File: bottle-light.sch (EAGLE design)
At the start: 49 parts, among them IC1 STM32F334K8T, IC2 LF33, T1 BC337, T2 BC337, T3 BC337

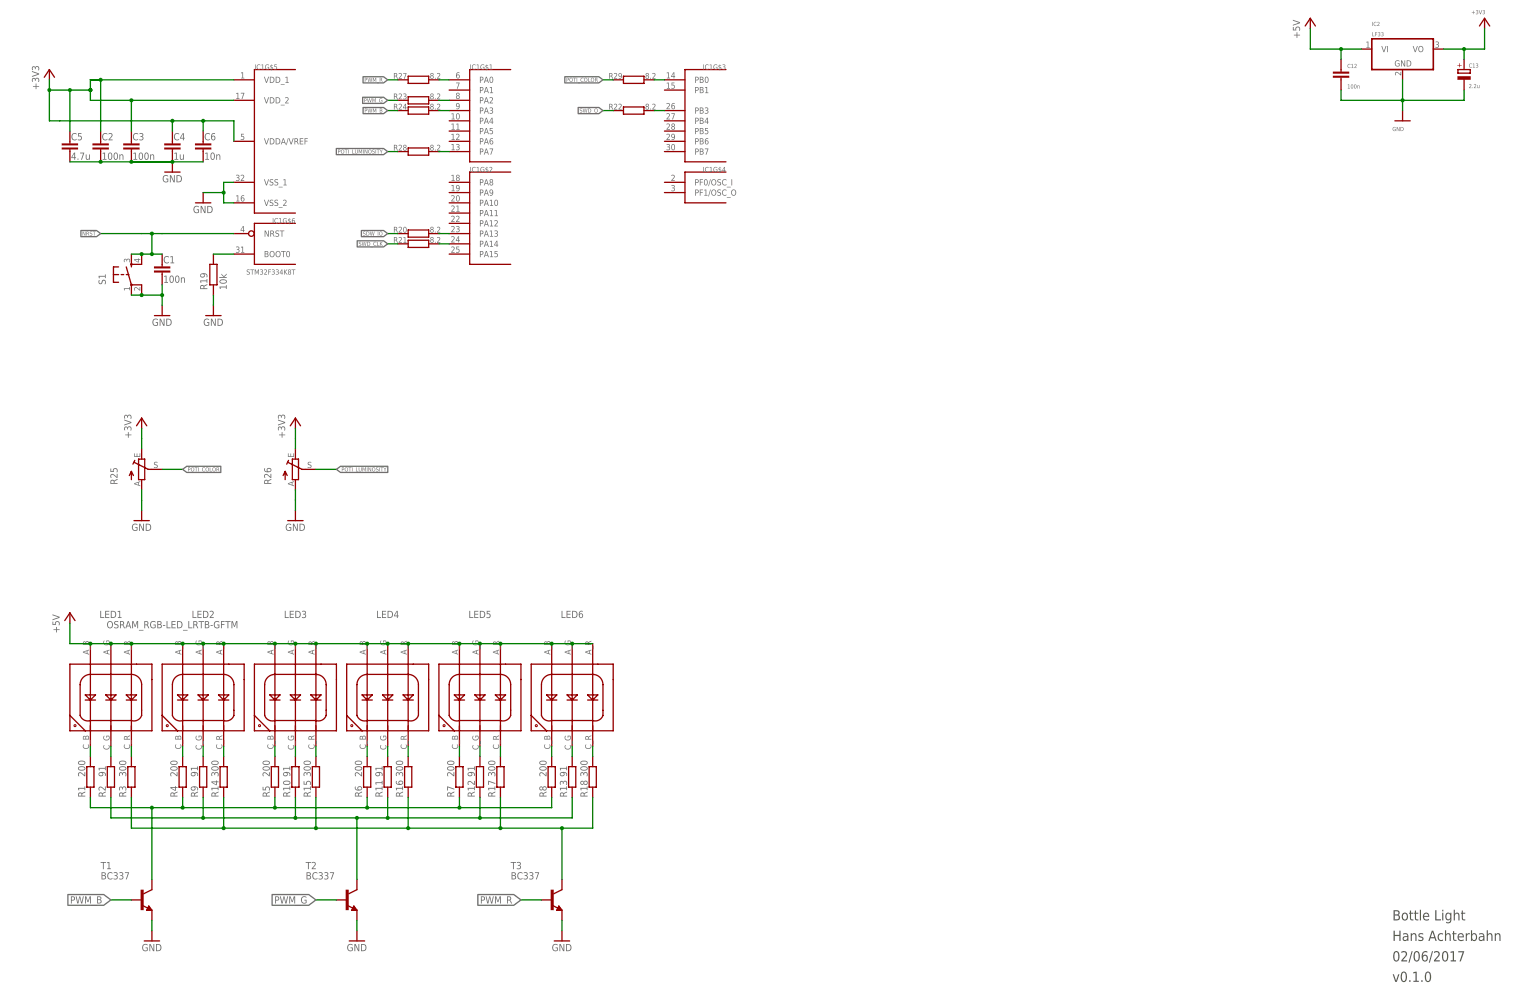
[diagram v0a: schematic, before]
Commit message: v0.1.1 worked on circuit diagram - new push buttons - new on/off button
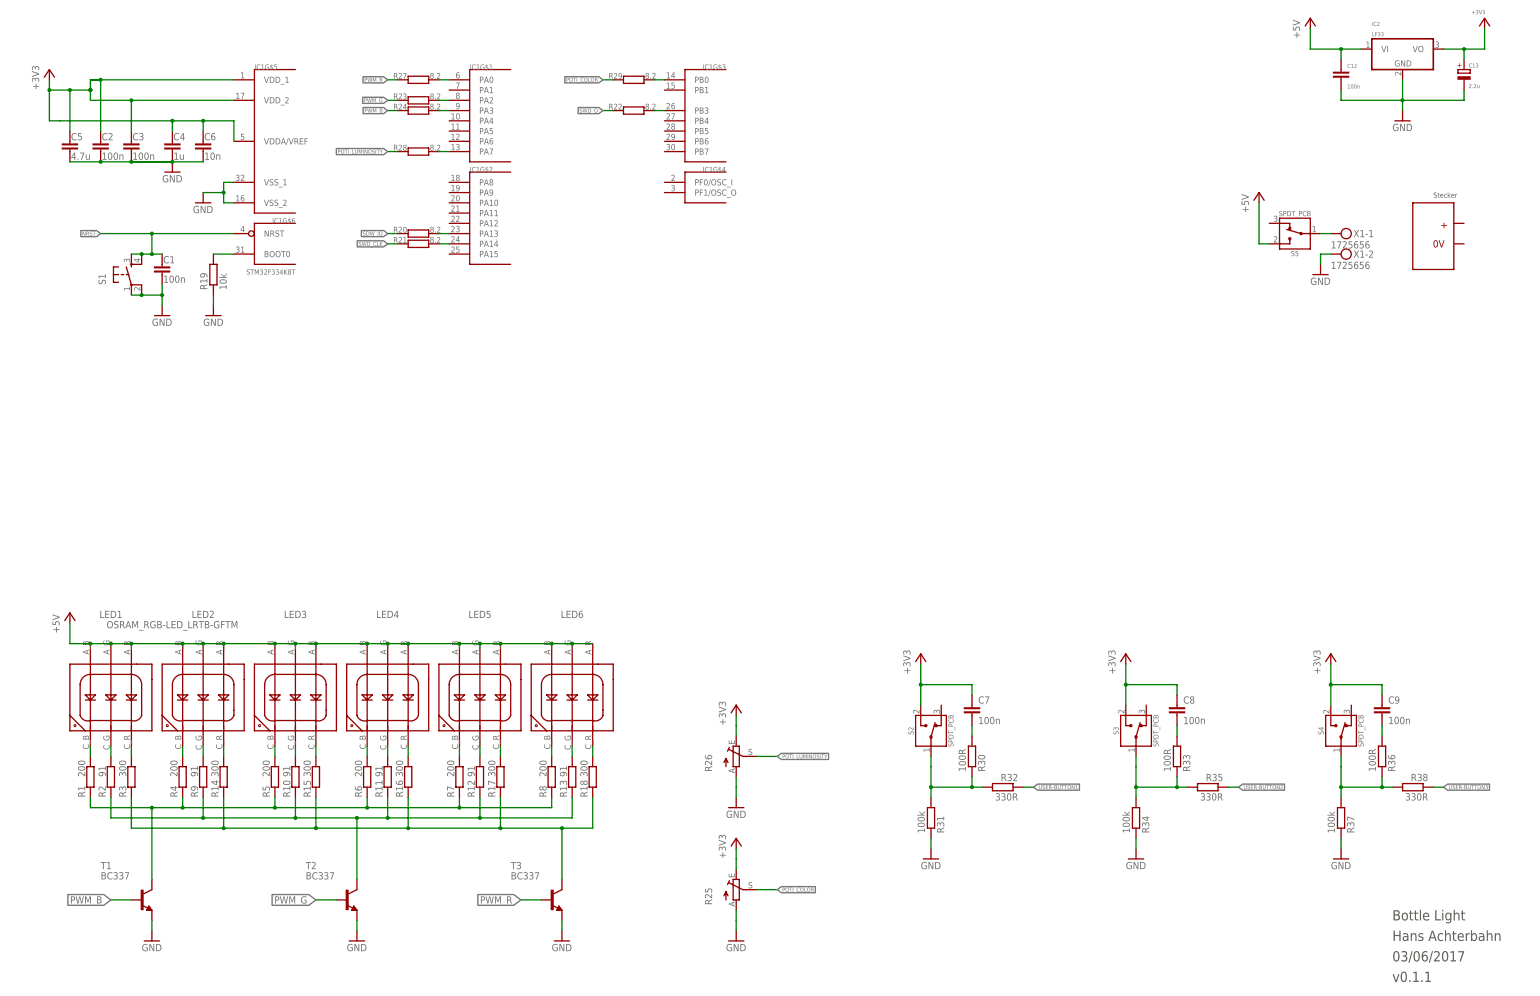
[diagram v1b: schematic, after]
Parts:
- added C7, C8, C9: 100n, resistor:C-EUC0603
- added R30, R33, R36: 100R, rcl:R-EU_R0603
- added R31, R34, R37: 100k, rcl:R-EU_R0603
- added R32, R35, R38: 330R, rcl:R-EU_R0603
- added S2, S3, S4, S5: SPDT_PCB, h8-switch:SPDT_PCB
- added X1: 1725656, con-phoenix-508:MKDSN1,5/2-5,08
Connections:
- new net N$30: R30.1, R31.2, R32.2, S2.1
- new net N$31: C7.2, R30.2
- new net N$32: R33.1, R34.2, R35.2, S3.1
- new net N$33: C8.2, R33.2
- new net N$35: R36.1, R37.2, R38.2, S4.1
- new net N$36: C9.2, R36.2
- new net N$37: S5.1, X1-1.KL
- new net USER-BUTTON1: R32.1
- new net USER-BUTTON2: R35.1
- new net USER-BUTTON3: R38.1
- net +3V3: now also C7.1, C8.1, C9.1, S2.2, S3.2, S4.2
- net +5V: now also S5.2
- net GND: now also R31.1, R34.1, R37.1, X1-2.KL
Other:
- note added: "03/06/2017"
- note added: "Stecker"
- note added: "v0.1.1"
- note removed: "02/06/2017"
- note removed: "v0.1.0"
- moved on the sheet: R25, R26

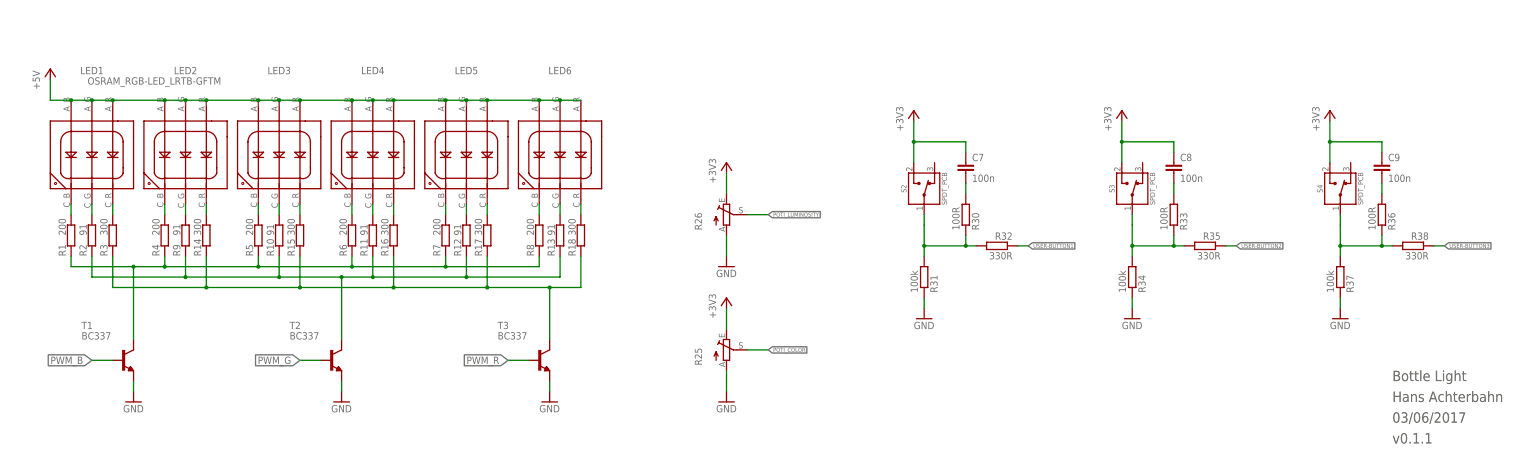
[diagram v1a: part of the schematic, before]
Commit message: v0.1.2 Put in new devices and began routing pcb - new potis - made groundplane size for case - placed leds, potis and switch
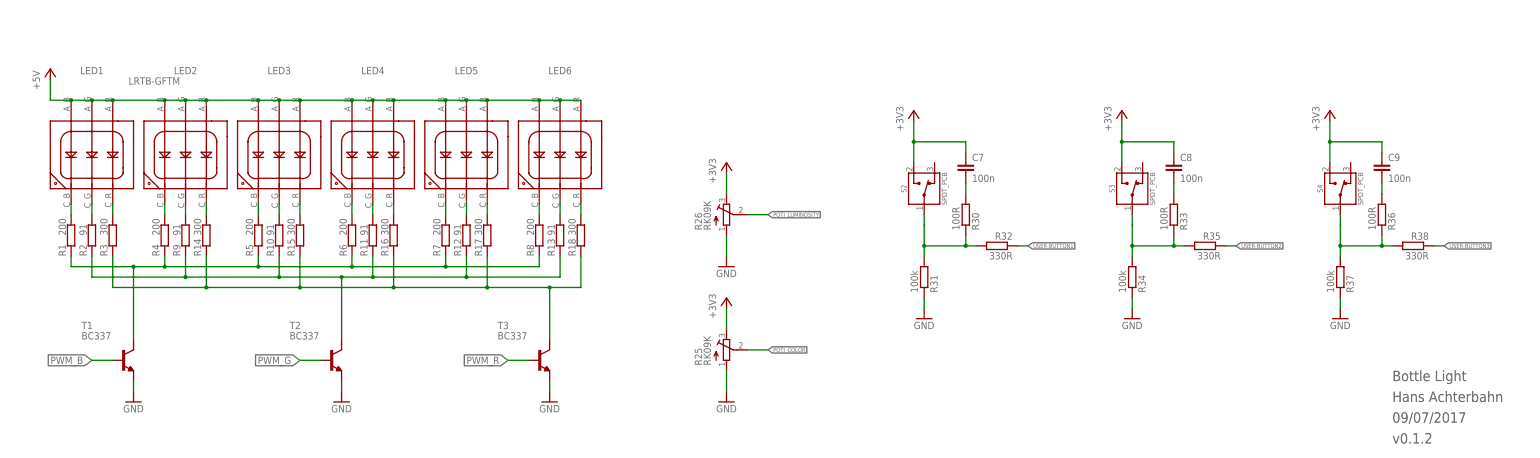
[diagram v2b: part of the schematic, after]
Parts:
- LED1, LED2, LED3, LED4, LED5, LED6: value OSRAM_RGB-LED_LRTB-GFTM -> LRTB-GFTM
- R25, R26: value (none) -> RK09K; device pot:TRIM_EU-CIP20C-6MM -> h8-rlc:POT_RK09K
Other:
- note added: "09/07/2017"
- note added: "v0.1.2"
- note removed: "03/06/2017"
- note removed: "v0.1.1"
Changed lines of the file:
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@@
 <part name="T3" library="transistor" deviceset="BC337" device=""/>
 <part name="IC1" library="h8-stm32" deviceset="STM32F334K8T" device=""/>
-<part name="LED1" library="h8-optic" deviceset="OSRAM_RGB-LED_LRTB-GFTM" device="">
+<part name="LED1" library="h8-optic" deviceset="OSRAM_RGB-LED_LRTB-GFTM" device="" value="LRTB-GFTM">
 <attribute name="MF" value="Osram"/>
 <attribute name="MFN" value="LRTB GFTM"/>
@@
 <attribute name="RS-ONLINE" value="830-6340"/>
 </part>
-<part name="LED2" library="h8-optic" deviceset="OSRAM_RGB-LED_LRTB-GFTM" device="">
+<part name="LED2" library="h8-optic" deviceset="OSRAM_RGB-LED_LRTB-GFTM" device="" value="LRTB-GFTM">
 <attribute name="MF" value="Osram"/>
 <attribute name="MFN" value="LRTB GFTM"/>
 <attribute name="RS-ONLINE" value="708-0725"/>
 </part>
-<part name="LED3" library="h8-optic" deviceset="OSRAM_RGB-LED_LRTB-GFTM" device="">
+<part name="LED3" library="h8-optic" deviceset="OSRAM_RGB-LED_LRTB-GFTM" device="" value="LRTB-GFTM">
 <attribute name="MF" value="Osram"/>
 <attribute name="MFN" value="LRTB GFTM"/>
 <attribute name="RS-ONLINE" value="708-0725"/>
 </part>
-<part name="LED4" library="h8-optic" deviceset="OSRAM_RGB-LED_LRTB-GFTM" device="">
+<part name="LED4" library="h8-optic" deviceset="OSRAM_RGB-LED_LRTB-GFTM" device="" value="LRTB-GFTM">
 <attribute name="MF" value="Osram"/>
 <attribute name="MFN" value="LRTB GFTM"/>
 <attribute name="RS-ONLINE" value="708-0725"/>
 </part>
-<part name="LED5" library="h8-optic" deviceset="OSRAM_RGB-LED_LRTB-GFTM" device="">
+<part name="LED5" library="h8-optic" deviceset="OSRAM_RGB-LED_LRTB-GFTM" device="" value="LRTB-GFTM">
 <attribute name="MF" value="Osram"/>
 <attribute name="MFN" value="LRTB GFTM"/>
 <attribute name="RS-ONLINE" value="708-0725"/>
 </part>
-<part name="LED6" library="h8-optic" deviceset="OSRAM_RGB-LED_LRTB-GFTM" device="">
+<part name="LED6" library="h8-optic" deviceset="OSRAM_RGB-LED_LRTB-GFTM" device="" value="LRTB-GFTM">
 <attribute name="MF" value="Osram"/>
 <attribute name="MFN" value="LRTB GFTM"/>
@@
 <part name="GND9" library="supply1" deviceset="GND" device=""/>
 <part name="+3V4" library="supply1" deviceset="+3V3" device=""/>
-<part name="R25" library="pot" deviceset="TRIM_EU-" device="CIP20C-6MM"/>
-<part name="R26" library="pot" deviceset="TRIM_EU-" device="CIP20C-6MM"/>
+<part name="R25" library="h8-rlc" deviceset="POT_RK09K" device="" value="RK09K"/>
+<part name="R26" library="h8-rlc" deviceset="POT_RK09K" device="" value="RK09K"/>
 <part name="R23" library="resistor" deviceset="R-EU_" device="R0603" value="8.2">
 <attribute name="RS-ONLINE" value="904-5027"/>
@@
 <text x="347.98" y="20.32" size="2.54" layer="97">Bottle Light</text>
 <text x="347.98" y="15.24" size="2.54" layer="97">Hans Achterbahn</text>
-<text x="347.98" y="10.16" size="2.54" layer="97">03/06/2017</text>
-<text x="347.98" y="5.08" size="2.54" layer="97">v0.1.1</text>
+<text x="347.98" y="10.16" size="2.54" layer="97">09/07/2017</text>
+<text x="347.98" y="5.08" size="2.54" layer="97">v0.1.2</text>
 <text x="358.14" y="199.39" size="1.27" layer="97">Stecker</text>
 </plain>
@@
 <instance part="GND9" gate="1" x="185.42" y="48.26"/>
 <instance part="+3V4" gate="G$1" x="185.42" y="73.66"/>
-<instance part="R25" gate="1" x="185.42" y="27.94"/>
-<instance part="R26" gate="1" x="185.42" y="60.96"/>
+<instance part="R25" gate="G$1" x="185.42" y="27.94"/>
+<instance part="R26" gate="G$1" x="185.42" y="60.96"/>
 <instance part="R23" gate="G$1" x="106.68" y="223.52" smashed="yes">
 <attribute name="NAME" x="103.886" y="223.774" size="1.4224" layer="95" rot="MR0"/>
@@
 <pinref part="GND8" gate="1" pin="GND"/>
 <wire x1="185.42" y1="20.32" x2="185.42" y2="17.78" width="0.1524" layer="91"/>
-<pinref part="R25" gate="1" pin="A"/>
+<pinref part="R25" gate="G$1" pin="A"/>
 <wire x1="185.42" y1="22.86" x2="185.42" y2="20.32" width="0.1524" layer="91"/>
 </segment>
@@
 <pinref part="GND9" gate="1" pin="GND"/>
 <wire x1="185.42" y1="50.8" x2="185.42" y2="53.34" width="0.1524" layer="91"/>
-<pinref part="R26" gate="1" pin="A"/>
+<pinref part="R26" gate="G$1" pin="A"/>
 <wire x1="185.42" y1="53.34" x2="185.42" y2="55.88" width="0.1524" layer="91"/>
 </segment>
@@
 <pinref part="+3V3" gate="G$1" pin="+3V3"/>
 <wire x1="185.42" y1="38.1" x2="185.42" y2="35.56" width="0.1524" layer="91"/>
-<pinref part="R25" gate="1" pin="E"/>
+<pinref part="R25" gate="G$1" pin="E"/>
 <wire x1="185.42" y1="33.02" x2="185.42" y2="35.56" width="0.1524" layer="91"/>
 </segment>
@@
 <pinref part="+3V4" gate="G$1" pin="+3V3"/>
 <wire x1="185.42" y1="68.58" x2="185.42" y2="71.12" width="0.1524" layer="91"/>
-<pinref part="R26" gate="1" pin="E"/>
+<pinref part="R26" gate="G$1" pin="E"/>
 <wire x1="185.42" y1="66.04" x2="185.42" y2="68.58" width="0.1524" layer="91"/>
 </segment>
@@
 <wire x1="190.5" y1="27.94" x2="195.58" y2="27.94" width="0.1524" layer="91"/>
 <label x="195.58" y="27.94" size="1.016" layer="95" xref="yes"/>
-<pinref part="R25" gate="1" pin="S"/>
+<pinref part="R25" gate="G$1" pin="S"/>
 </segment>
 <segment>
@@
 <wire x1="190.5" y1="60.96" x2="195.58" y2="60.96" width="0.1524" layer="91"/>
 <label x="195.58" y="60.96" size="1.016" layer="95" xref="yes"/>
-<pinref part="R26" gate="1" pin="S"/>
-</segment>
-<segment>
+<pinref part="R26" gate="G$1" pin="S"/>
+</segment>
+<segment>
